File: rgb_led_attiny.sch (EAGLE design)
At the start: 14 parts, among them IC1 ATTINY45-20PU, IC2 MC7805BTG, Q1 IRF540NPBF, Q2 IRF540NPBF, Q3 IRF540NPBF

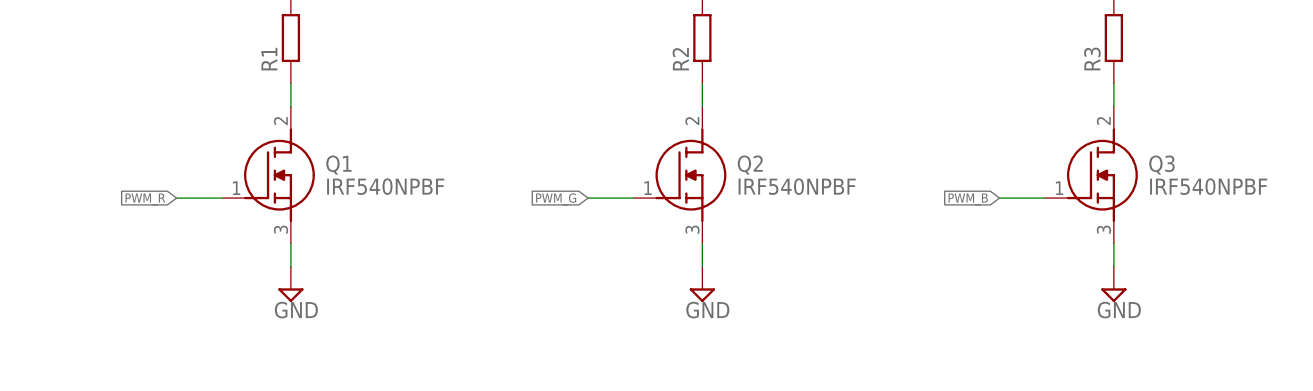
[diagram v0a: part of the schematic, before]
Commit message: Deuxième routage, plus compact avecles resistances en vertical. Ajout de pull-down sur le gate des MOSFETs
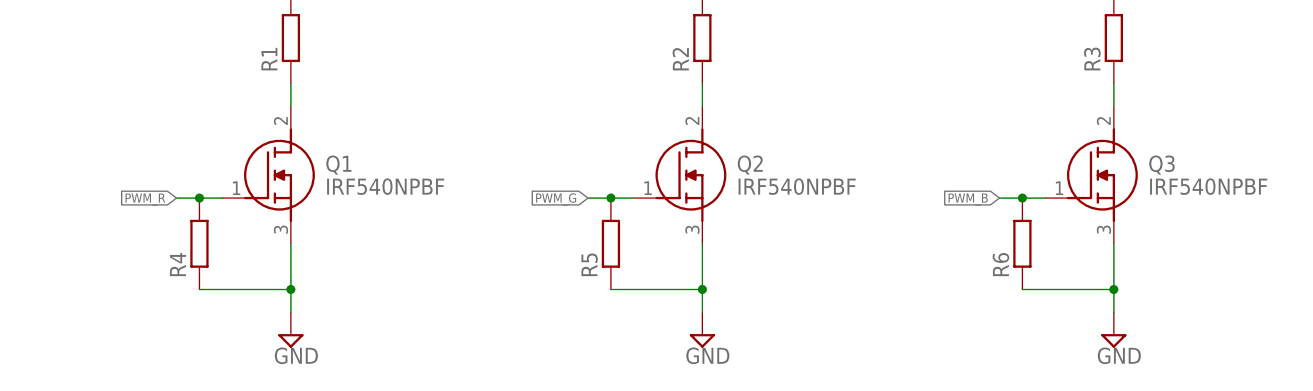
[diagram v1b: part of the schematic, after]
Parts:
- added R4, R5, R6: (no value), rcl:R-EU_0207/10
- R1, R2, R3: device rcl:R-EU_0613/15 -> rcl:R-EU_0613/5V
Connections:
- net GND: now also R4.1, R5.1, R6.1
- net PWM_B: now also R6.2
- net PWM_G: now also R5.2
- net PWM_R: now also R4.2
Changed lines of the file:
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@@
 <part name="Q1" library="rgb_led_attiny" deviceset="IRF540NPBF" device=""/>
 <part name="SUPPLY4" library="supply2" library_urn="urn:adsk.eagle:library:372" deviceset="GND" device=""/>
-<part name="R1" library="rcl" library_urn="urn:adsk.eagle:library:334" deviceset="R-EU_" device="0613/15" package3d_urn="urn:adsk.eagle:package:23581/1"/>
+<part name="R1" library="rcl" library_urn="urn:adsk.eagle:library:334" deviceset="R-EU_" device="0613/5V" package3d_urn="urn:adsk.eagle:package:23582/1"/>
 <part name="JP2" library="pinhead" library_urn="urn:adsk.eagle:library:325" deviceset="PINHD-1X2" device="" package3d_urn="urn:adsk.eagle:package:22435/2"/>
 <part name="Q2" library="rgb_led_attiny" deviceset="IRF540NPBF" device=""/>
 <part name="SUPPLY5" library="supply2" library_urn="urn:adsk.eagle:library:372" deviceset="GND" device=""/>
-<part name="R2" library="rcl" library_urn="urn:adsk.eagle:library:334" deviceset="R-EU_" device="0613/15" package3d_urn="urn:adsk.eagle:package:23581/1"/>
+<part name="R2" library="rcl" library_urn="urn:adsk.eagle:library:334" deviceset="R-EU_" device="0613/5V" package3d_urn="urn:adsk.eagle:package:23582/1"/>
 <part name="JP3" library="pinhead" library_urn="urn:adsk.eagle:library:325" deviceset="PINHD-1X2" device="" package3d_urn="urn:adsk.eagle:package:22435/2"/>
 <part name="Q3" library="rgb_led_attiny" deviceset="IRF540NPBF" device=""/>
 <part name="SUPPLY6" library="supply2" library_urn="urn:adsk.eagle:library:372" deviceset="GND" device=""/>
-<part name="R3" library="rcl" library_urn="urn:adsk.eagle:library:334" deviceset="R-EU_" device="0613/15" package3d_urn="urn:adsk.eagle:package:23581/1"/>
+<part name="R3" library="rcl" library_urn="urn:adsk.eagle:library:334" deviceset="R-EU_" device="0613/5V" package3d_urn="urn:adsk.eagle:package:23582/1"/>
 <part name="JP4" library="pinhead" library_urn="urn:adsk.eagle:library:325" deviceset="PINHD-1X2" device="" package3d_urn="urn:adsk.eagle:package:22435/2"/>
+<part name="R4" library="rcl" library_urn="urn:adsk.eagle:library:334" deviceset="R-EU_" device="0207/10" package3d_urn="urn:adsk.eagle:package:23491/1"/>
+<part name="R5" library="rcl" library_urn="urn:adsk.eagle:library:334" deviceset="R-EU_" device="0207/10" package3d_urn="urn:adsk.eagle:package:23491/1"/>
+<part name="R6" library="rcl" library_urn="urn:adsk.eagle:library:334" deviceset="R-EU_" device="0207/10" package3d_urn="urn:adsk.eagle:package:23491/1"/>
 </parts>
 <sheets>
@@
 <attribute name="VALUE" x="123.19" y="26.67" size="1.778" layer="96" align="center-left"/>
 </instance>
-<instance part="SUPPLY4" gate="GND" x="119.38" y="15.24" smashed="yes">
-<attribute name="VALUE" x="117.475" y="12.065" size="1.778" layer="96"/>
+<instance part="SUPPLY4" gate="GND" x="119.38" y="10.16" smashed="yes">
+<attribute name="VALUE" x="117.475" y="6.985" size="1.778" layer="96"/>
 </instance>
 <instance part="R1" gate="G$1" x="119.38" y="43.18" smashed="yes" rot="R90">
@@
 <attribute name="VALUE" x="168.91" y="26.67" size="1.778" layer="96" align="center-left"/>
 </instance>
-<instance part="SUPPLY5" gate="GND" x="165.1" y="15.24" smashed="yes">
-<attribute name="VALUE" x="163.195" y="12.065" size="1.778" layer="96"/>
+<instance part="SUPPLY5" gate="GND" x="165.1" y="10.16" smashed="yes">
+<attribute name="VALUE" x="163.195" y="6.985" size="1.778" layer="96"/>
 </instance>
 <instance part="R2" gate="G$1" x="165.1" y="43.18" smashed="yes" rot="R90">
@@
 <attribute name="VALUE" x="214.63" y="26.67" size="1.778" layer="96" align="center-left"/>
 </instance>
-<instance part="SUPPLY6" gate="GND" x="210.82" y="15.24" smashed="yes">
-<attribute name="VALUE" x="208.915" y="12.065" size="1.778" layer="96"/>
+<instance part="SUPPLY6" gate="GND" x="210.82" y="10.16" smashed="yes">
+<attribute name="VALUE" x="208.915" y="6.985" size="1.778" layer="96"/>
 </instance>
 <instance part="R3" gate="G$1" x="210.82" y="43.18" smashed="yes" rot="R90">
@@
 <attribute name="NAME" x="222.25" y="50.165" size="1.778" layer="95" rot="R180"/>
 <attribute name="VALUE" x="222.25" y="60.96" size="1.778" layer="96" rot="R180"/>
+</instance>
+<instance part="R4" gate="G$1" x="109.22" y="20.32" smashed="yes" rot="R90">
+<attribute name="NAME" x="107.7214" y="16.51" size="1.778" layer="95" rot="R90"/>
+<attribute name="VALUE" x="112.522" y="16.51" size="1.778" layer="96" rot="R90"/>
+</instance>
+<instance part="R5" gate="G$1" x="154.94" y="20.32" smashed="yes" rot="R90">
+<attribute name="NAME" x="153.4414" y="16.51" size="1.778" layer="95" rot="R90"/>
+<attribute name="VALUE" x="158.242" y="16.51" size="1.778" layer="96" rot="R90"/>
+</instance>
+<instance part="R6" gate="G$1" x="200.66" y="20.32" smashed="yes" rot="R90">
+<attribute name="NAME" x="199.1614" y="16.51" size="1.778" layer="95" rot="R90"/>
+<attribute name="VALUE" x="203.962" y="16.51" size="1.778" layer="96" rot="R90"/>
 </instance>
 </instances>
@@
 <pinref part="SUPPLY4" gate="GND" pin="GND"/>
 <pinref part="Q1" gate="G$1" pin="S"/>
-<wire x1="119.38" y1="17.78" x2="119.38" y2="20.32" width="0.1524" layer="91"/>
+<wire x1="119.38" y1="12.7" x2="119.38" y2="15.24" width="0.1524" layer="91"/>
+<pinref part="R4" gate="G$1" pin="1"/>
+<wire x1="119.38" y1="15.24" x2="119.38" y2="20.32" width="0.1524" layer="91"/>
+<wire x1="109.22" y1="15.24" x2="119.38" y2="15.24" width="0.1524" layer="91"/>
+<junction x="119.38" y="15.24"/>
 </segment>
 <segment>
 <pinref part="SUPPLY5" gate="GND" pin="GND"/>
 <pinref part="Q2" gate="G$1" pin="S"/>
-<wire x1="165.1" y1="17.78" x2="165.1" y2="20.32" width="0.1524" layer="91"/>
+<wire x1="165.1" y1="12.7" x2="165.1" y2="15.24" width="0.1524" layer="91"/>
+<pinref part="R5" gate="G$1" pin="1"/>
+<wire x1="165.1" y1="15.24" x2="165.1" y2="20.32" width="0.1524" layer="91"/>
+<wire x1="154.94" y1="15.24" x2="165.1" y2="15.24" width="0.1524" layer="91"/>
+<junction x="165.1" y="15.24"/>
 </segment>
 <segment>
 <pinref part="SUPPLY6" gate="GND" pin="GND"/>
 <pinref part="Q3" gate="G$1" pin="S"/>
-<wire x1="210.82" y1="17.78" x2="210.82" y2="20.32" width="0.1524" layer="91"/>
+<wire x1="210.82" y1="12.7" x2="210.82" y2="15.24" width="0.1524" layer="91"/>
+<pinref part="R6" gate="G$1" pin="1"/>
+<wire x1="210.82" y1="15.24" x2="210.82" y2="20.32" width="0.1524" layer="91"/>
+<wire x1="200.66" y1="15.24" x2="210.82" y2="15.24" width="0.1524" layer="91"/>
+<junction x="210.82" y="15.24"/>
 </segment>
 </net>
@@
 <segment>
 <pinref part="Q3" gate="G$1" pin="G"/>
-<wire x1="203.2" y1="25.4" x2="198.12" y2="25.4" width="0.1524" layer="91"/>
+<wire x1="203.2" y1="25.4" x2="200.66" y2="25.4" width="0.1524" layer="91"/>
 <label x="198.12" y="25.4" size="1.016" layer="95" rot="R180" xref="yes"/>
+<pinref part="R6" gate="G$1" pin="2"/>
+<wire x1="200.66" y1="25.4" x2="198.12" y2="25.4" width="0.1524" layer="91"/>
+<junction x="200.66" y="25.4"/>
 </segment>
 </net>
@@
 <segment>
 <pinref part="Q2" gate="G$1" pin="G"/>
-<wire x1="157.48" y1="25.4" x2="152.4" y2="25.4" width="0.1524" layer="91"/>
+<wire x1="157.48" y1="25.4" x2="154.94" y2="25.4" width="0.1524" layer="91"/>
 <label x="152.4" y="25.4" size="1.016" layer="95" rot="R180" xref="yes"/>
+<pinref part="R5" gate="G$1" pin="2"/>
+<wire x1="154.94" y1="25.4" x2="152.4" y2="25.4" width="0.1524" layer="91"/>
+<junction x="154.94" y="25.4"/>
 </segment>
 </net>
@@
 <segment>
 <pinref part="Q1" gate="G$1" pin="G"/>
-<wire x1="111.76" y1="25.4" x2="106.68" y2="25.4" width="0.1524" layer="91"/>
+<wire x1="111.76" y1="25.4" x2="109.22" y2="25.4" width="0.1524" layer="91"/>
 <label x="106.68" y="25.4" size="1.016" layer="95" rot="R180" xref="yes"/>
-</segment>
-</net>
+<pinref part="R4" gate="G$1" pin="2"/>
+<wire x1="109.22" y1="25.4" x2="106.68" y2="25.4" width="0.1524" layer="91"/>
+<junction x="109.22" y="25.4"/>
+</segment>
+</net>
